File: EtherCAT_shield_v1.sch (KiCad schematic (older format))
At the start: 20 parts, among them J1 RJ45-PULSETRANS, J2 RJ45-PULSETRANS, P1 CONN_02X10, P2 CONN_02X19, P3 CONN_02X19, U1 LAN9252

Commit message: GPIOのLED並べた 実質完成
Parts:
- added D10, D11, D12, D13, D14, D15, D16, D17, D18, D3, D4, D5, D6, D7, D8, D9: LED, LEDs:LED_0603, symbol LED
- added J3, J4, J5, J6: GS3, Connect:GS3, symbol GS3
- added J7, J8: GS2, Connect:GS2, symbol GS2
- added R24, R25, R26, R27, R28, R29, R30, R31, R32, R33, R34, R35, R36, R37, R38, R39: 1k, Resistors_SMD:R_0603, symbol R
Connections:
- net +3V3: now also R23.2; no longer R23.1
- net +5V: now also P2.18 (P18); no longer P2.6 (P6)
- net GND: now also D10.1 (K), D11.1 (K), D12.1 (K), D13.1 (K), D14.1 (K), D15.1 (K), D16.1 (K), D17.1 (K), D18.1 (K), D3.1 (K), D4.1 (K), D5.1 (K), D6.1 (K), D7.1 (K), D8.1 (K), D9.1 (K)
- net SCK: now also J4.2 (G2); no longer P3.22 (P22)
- net SIO0: now also J6.2 (G2); no longer P3.1 (P1)
- net SIO1: now also J5.2 (G2); no longer P2.1 (P1)
- net ~SCS: now also J3.2 (G2); no longer P3.17 (P17)
- net at J2.11 (LEDY_A): now also R23.1; no longer R23.2
- net SIO2: now reaches U1.12 (SIO2)
- net SIO2: now also J7.1 (G1)
- net GPIO8: now reaches P1.18 (P18), U1.15 (GPIO8)
- net GPIO8: now also R32.2
- net GPIO0: now reaches P1.17 (P17)
- net GPIO0: now also U1.36 (GPIO0), R24.2; no longer U1.16 (GPIO7)
- net SYNC1: now reaches P2.27 (P27), U1.18 (SYNC1/LATCH1)
- net GPIO1: now reaches P1.15 (P15)
- net GPIO1: now also U1.39 (GPIO1), R25.2; no longer U1.21 (GPIO6)
- net GPIO2: now reaches P1.13 (P13)
- net GPIO2: now also U1.40 (GPIO2), R26.2; no longer U1.22 (GPIO5)
- net GPIO3: now reaches P1.11 (P11)
- net GPIO3: now also U1.49 (GPIO3), R27.2; no longer U1.23 (GPIO4)
- net GPIO11: now reaches P1.12 (P12), U1.26 (GPIO11)
- net GPIO11: now also R35.2
- net GPIO12: now reaches P1.10 (P10), U1.27 (GPIO12)
- net GPIO12: now also R36.2
- net GPIO13: now reaches P1.8 (P8), U1.28 (GPIO13)
- net GPIO13: now also R37.2
- net GPIO10: now reaches P1.14 (P14), U1.29 (GPIO10)
- net GPIO10: now also R34.2
- net GPIO14: now reaches P1.6 (P6), U1.30 (GPIO14)
- net GPIO14: now also R38.2
- net GPIO15: now reaches P1.4 (P4), U1.31 (GPIO15)
- net GPIO15: now also R39.2
- net GPIO9: now reaches P1.16 (P16), U1.33 (GPIO9)
- net GPIO9: now also R33.2
- net SYNC0: now reaches P2.25 (P25), U1.34 (SYNC0/LATCH0)
- net SIO3: now reaches U1.35 (SIO3)
- net SIO3: now also J8.1 (G1)
- net GPIO7: now reaches P1.3 (P3)
- net GPIO7: now also U1.16 (GPIO7), R31.2; no longer U1.36 (GPIO0)
- net GPIO6: now reaches P1.5 (P5)
- net GPIO6: now also U1.21 (GPIO6), R30.2; no longer U1.39 (GPIO1)
- net GPIO5: now reaches P1.7 (P7)
- net GPIO5: now also U1.22 (GPIO5), R29.2; no longer U1.40 (GPIO2)
- net GPIO4: now reaches P1.9 (P9)
- net GPIO4: now also U1.23 (GPIO4), R28.2; no longer U1.49 (GPIO3)
- net PB0: now reaches P2.34 (P34)
- net PB0: now also J5.3 (G3)
- net PA6: now reaches P3.13 (P13)
- net PA6: now also J8.2 (G2)
- net PA7: now reaches P3.15 (P15)
- net PA7: now also J7.2 (G2)
- net PB11: now reaches P3.18 (P18)
- net PB11: now also J3.3 (G3)
- net PB1: now reaches P3.24 (P24)
- net PB1: now also J6.3 (G3)
- net PB10: now reaches P3.25 (P25)
- net PB10: now also J4.3 (G3)
- net LAN9252/IRQ renamed LAN9252_IRQ
- net LAN9252/~RST renamed LAN9252_RST
- new net: D3.2 (A), R24.1
- new net: D4.2 (A), R25.1
- new net: D5.2 (A), R26.1
- new net: D6.2 (A), R27.1
- new net: D7.2 (A), R28.1
- new net: D8.2 (A), R29.1
- new net: D9.2 (A), R30.1
- new net: D10.2 (A), R31.1
- new net: D11.2 (A), R32.1
- new net: D12.2 (A), R33.1
- new net: D13.2 (A), R34.1
- new net: D14.2 (A), R35.1
- new net: D15.2 (A), R36.1
- new net: D16.2 (A), R37.1
- new net: D17.2 (A), R38.1
- new net: D18.2 (A), R39.1
- new net PB2: J4.1 (G1), P3.22 (P22)
- new net PB6: J3.1 (G1), P3.17 (P17)
- new net PC10: J5.1 (G1), P2.1 (P1)
- new net PC9: J6.1 (G1), P3.1 (P1)
- no-connect marks 6 -> 5
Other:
- note added: "F446,F722_CLK"
- note added: "F446,F722_SIO0"
- note added: "F446,F722_SIO1"
- note added: "F446,F722_~SCS"
- note added: "L476"
- note added: "L476_CLK"
- note added: "L476_SIO0"
- note added: "L476_SIO1"
- note added: "L476_~SCS"
- note added: "Nucleo64 morpho Pin"
- moved on the sheet: C1, C2, C3, D1, D2, J1, J2, P1, P2, P3, R1, R2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

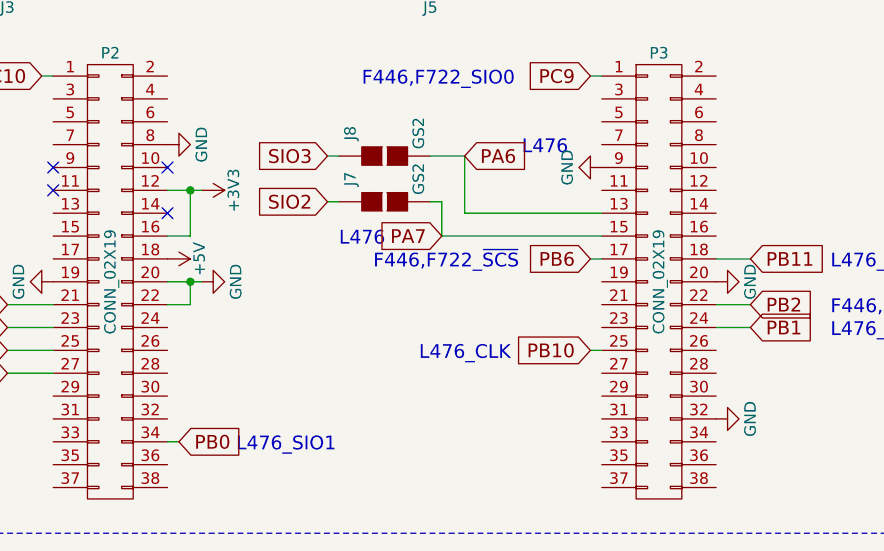
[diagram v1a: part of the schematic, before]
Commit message: 外形を変更
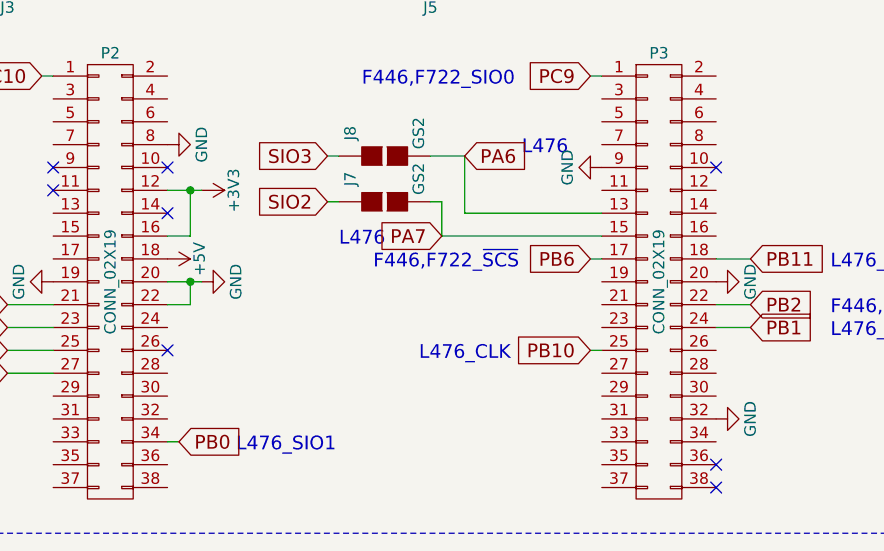
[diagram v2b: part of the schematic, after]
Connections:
- no-connect marks 5 -> 9
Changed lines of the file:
@@
 Text GLabel 4650 2900 0    60   Input ~ 0
 GPIO15
+NoConn ~ 2250 6900
+NoConn ~ 4650 7400
+NoConn ~ 4650 7500
+NoConn ~ 4650 6100
 $EndSCHEMATC

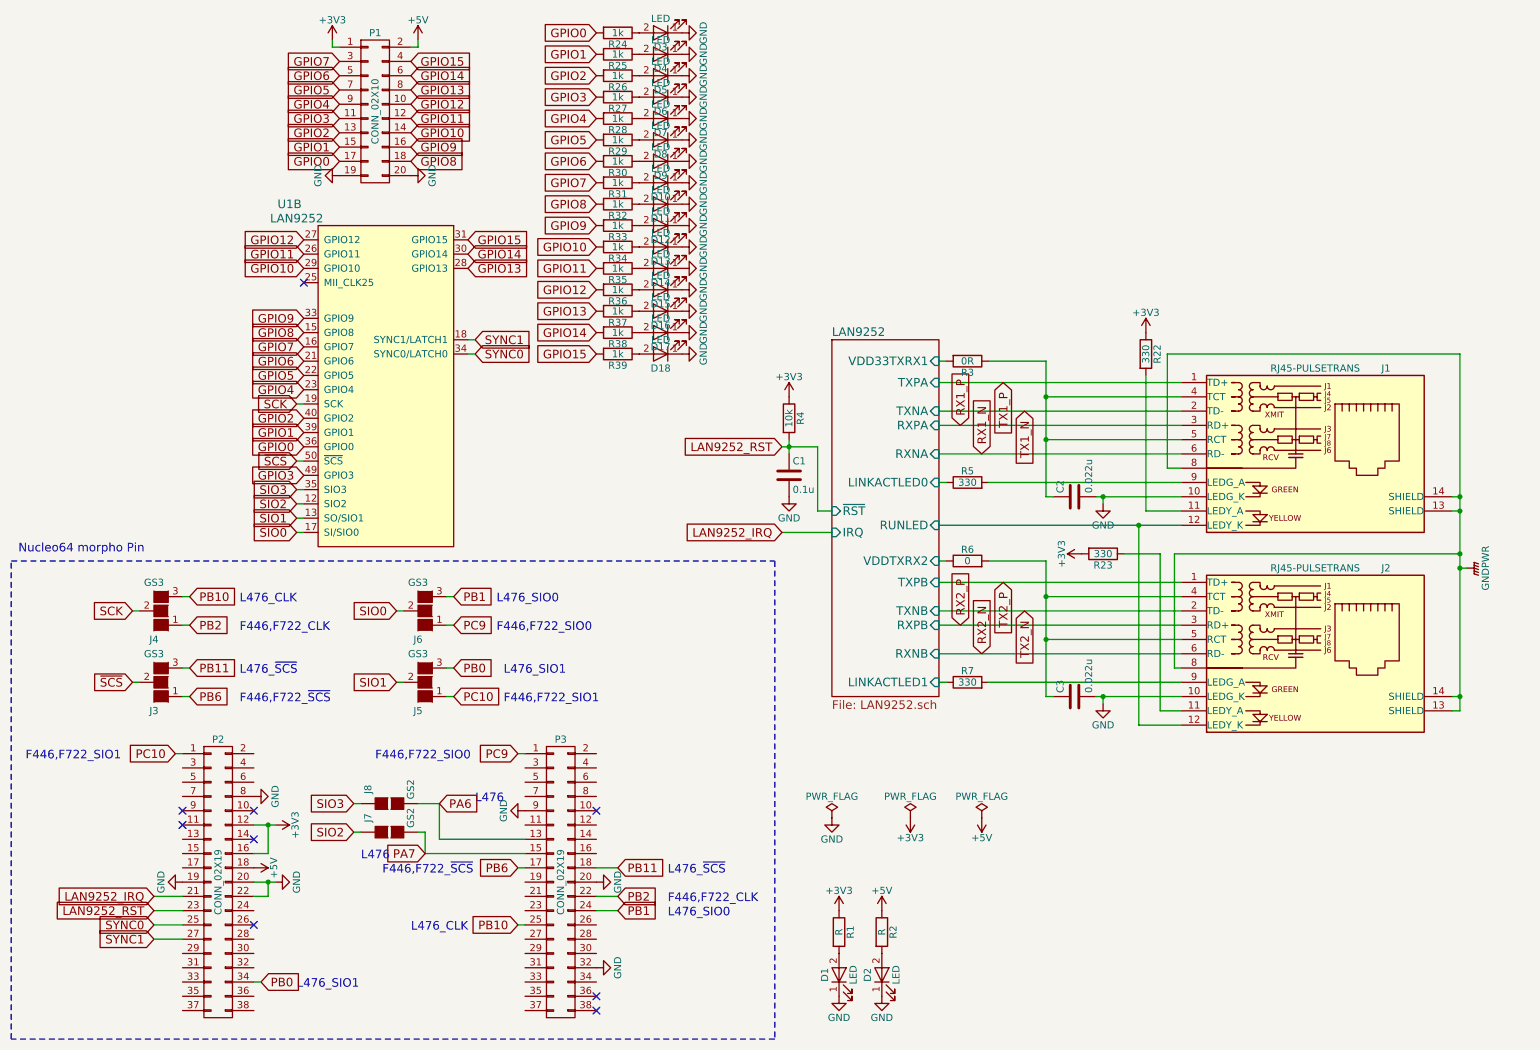
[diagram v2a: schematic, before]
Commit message: 外形線を変更
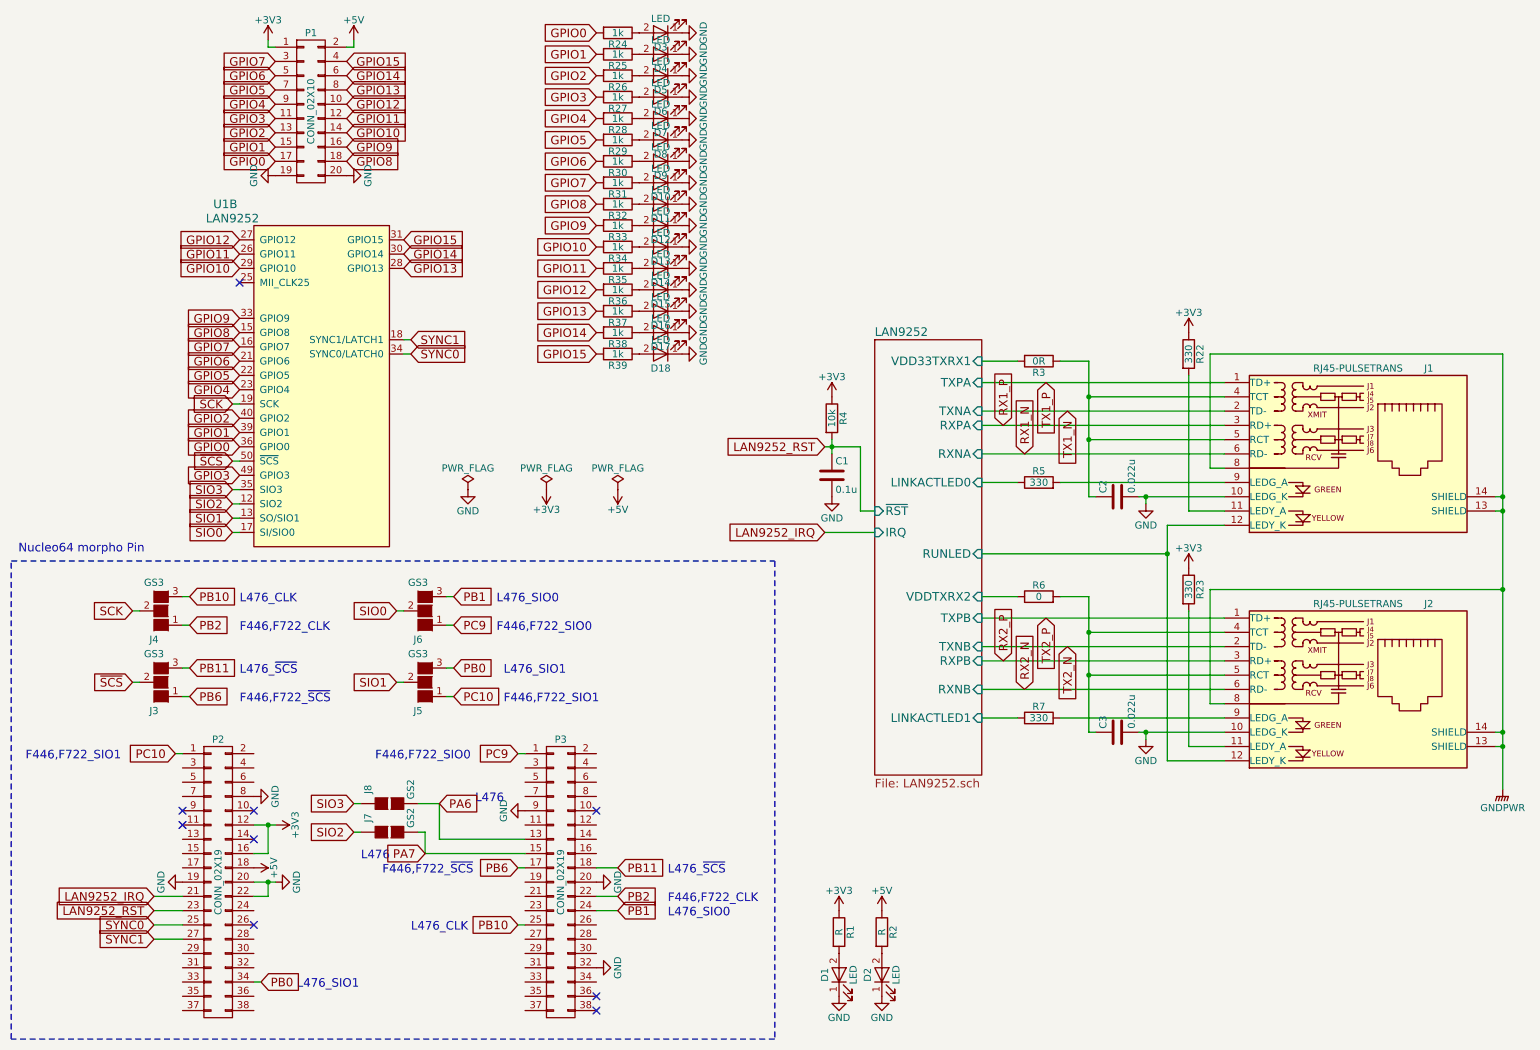
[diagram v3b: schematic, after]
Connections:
- net +3V3: now also R23.1; no longer R23.2
- net at J2.11 (LEDY_A): now also R23.2; no longer R23.1
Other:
- moved on the sheet: C1, C2, C3, J1, J2, P1, R22, R23, R3, R4, R5, R6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
